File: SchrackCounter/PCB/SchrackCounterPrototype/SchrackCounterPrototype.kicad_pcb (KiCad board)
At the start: 4 copper layers, 117.5 x 98 mm, 19 parts, among them J1 Conn_01x05_Pin, SW1 SW_Push, SW2 SW_Push, SW3 SW_Push, U1 ESP32-DEVKIT-V1

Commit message: SchrackMulticlock stolen code
Not mine, I stole it, its open source
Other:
- board text added: "add buzzer"
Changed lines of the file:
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@@
 		(tags "Through hole pin header THT 1x05 2.54mm single row")
 		(property "Reference" "J1"
-			(at 0 -2.33 360)
+			(at 0 -2.33 0)
 			(layer "F.SilkS")
 			(hide yes)
@@
 		)
 		(property "Value" "Conn_01x05_Pin"
-			(at 0 12.49 360)
+			(at 0 12.49 0)
 			(layer "F.Fab")
 			(effects
@@
 		(tags "C Disc series Radial pin pitch 5.00mm  diameter 6mm width 2.5mm Capacitor")
 		(property "Reference" "C2"
-			(at 2.5 -2.5 360)
+			(at 2.5 -2.5 0)
 			(layer "F.SilkS")
 			(hide yes)
@@
 		)
 		(property "Value" "100nF"
-			(at 2.5 2.5 360)
+			(at 2.5 2.5 0)
 			(layer "F.Fab")
 			(effects
@@
 		)
 		(fp_text user "${REFERENCE}"
-			(at 2.5 0 360)
+			(at 2.5 0 0)
 			(layer "F.Fab")
 			(effects
@@
 		(tags "CP Radial series Radial pin pitch 2.50mm  diameter 6.3mm Electrolytic Capacitor")
 		(property "Reference" "C1"
-			(at 1.25 -4.4 360)
+			(at 1.25 -4.4 0)
 			(layer "F.SilkS")
 			(hide yes)
@@
 		)
 		(property "Value" "10uF"
-			(at 1.25 4.4 360)
+			(at 1.25 4.4 0)
 			(layer "F.Fab")
 			(effects
@@
 		)
 		(fp_text user "${REFERENCE}"
-			(at 1.25 0 360)
+			(at 1.25 0 0)
 			(layer "F.Fab")
 			(effects
@@
 		(tags "tact sw push 6mm")
 		(property "Reference" "SW3"
-			(at 3.25 -2.25 360)
+			(at 3.25 -2.25 0)
 			(layer "F.SilkS")
 			(hide yes)
@@
 		)
 		(property "Value" "SW_Push"
-			(at 3.75 6.7 360)
+			(at 3.75 6.7 0)
 			(layer "F.Fab")
 			(effects
@@
 		)
 		(fp_text user "${REFERENCE}"
-			(at 3.25 2.25 360)
+			(at 3.25 2.25 0)
 			(layer "F.Fab")
 			(effects
@@
 		(tags "Resistor Axial_DIN0207 series Axial Horizontal pin pitch 10.16mm 0.25W = 1/4W length 6.3mm diameter 2.5mm")
 		(property "Reference" "R4"
-			(at 5 -2.37 360)
+			(at 5 -2.37 0)
 			(layer "F.SilkS")
 			(hide yes)
@@
 		)
 		(property "Value" "1k"
-			(at 5.08 2.37 360)
+			(at 5.08 2.37 0)
 			(layer "F.Fab")
 			(effects
@@
 		)
 		(fp_text user "${REFERENCE}"
-			(at 5.08 0 360)
+			(at 5.08 0 0)
 			(layer "F.Fab")
 			(effects
@@
 		(tags "tact sw push 6mm")
 		(property "Reference" "SW2"
-			(at 3.25 -2.25 360)
+			(at 3.25 -2.25 0)
 			(layer "F.SilkS")
 			(hide yes)
@@
 		)
 		(property "Value" "SW_Push"
-			(at 3.75 6.7 360)
+			(at 3.75 6.7 0)
 			(layer "F.Fab")
 			(effects
@@
 		)
 		(fp_text user "${REFERENCE}"
-			(at 3.25 2.25 360)
+			(at 3.25 2.25 0)
 			(layer "F.Fab")
 			(effects
@@
 		(tags "C Disc series Radial pin pitch 5.00mm  diameter 6mm width 2.5mm Capacitor")
 		(property "Reference" "C3"
-			(at 2.5 -2.5 360)
+			(at 2.5 -2.5 0)
 			(layer "F.SilkS")
 			(hide yes)
@@
 		)
 		(property "Value" "100nF"
-			(at 2.5 2.5 360)
+			(at 2.5 2.5 0)
 			(layer "F.Fab")
 			(effects
@@
 		)
 		(fp_text user "${REFERENCE}"
-			(at 2.5 0 360)
+			(at 2.5 0 0)
 			(layer "F.Fab")
 			(effects
@@
 		(tags "Through hole Samtec HPM power header series 11.94mm post length THT 1x02 5.08mm single row")
 		(property "Reference" "BT1"
-			(at 8.5 0.5 360)
+			(at 8.5 0.5 0)
 			(layer "B.SilkS")
 			(hide yes)
@@
 		)
 		(property "Value" "Battery"
-			(at 0.25 2.25 360)
+			(at 0.25 2.25 0)
 			(layer "B.Fab")
 			(effects
@@
 		)
 		(fp_text user "${REFERENCE}"
-			(at 11 -1.25 360)
+			(at 11 -1.25 0)
 			(layer "B.Fab")
 			(effects
@@
 		(layer "Edge.Cuts")
 	)
+	(gr_text "add buzzer"
+		(at 189.05 123.445 0)
+		(layer "Cmts.User")
+		(effects
+			(font
+				(size 1 1)
+				(thickness 0.15)
+			)
+			(justify left bottom)
+		)
+	)
 	(dimension

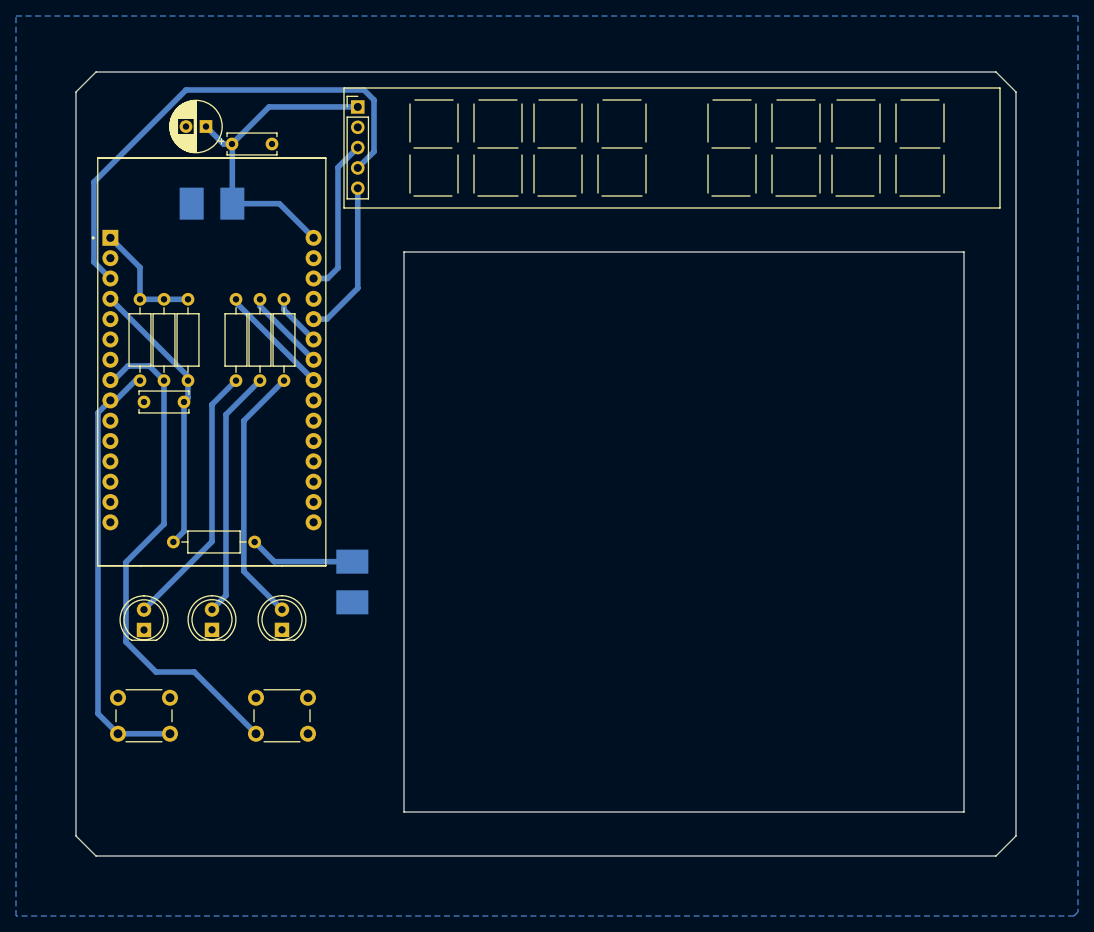
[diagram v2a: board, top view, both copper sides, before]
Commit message: Schrackcounter Prototype update
Schematic + PCB update, final version
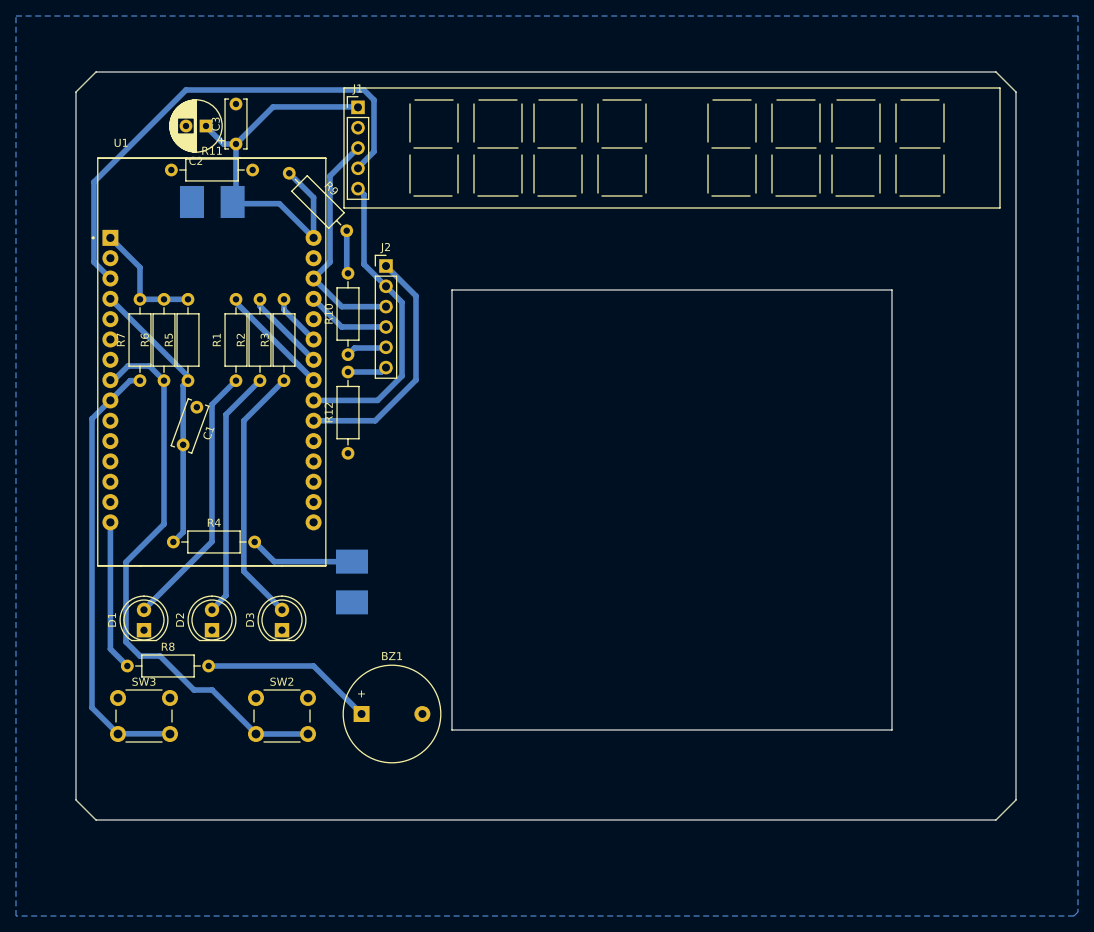
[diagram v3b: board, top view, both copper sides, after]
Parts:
- added BZ1: Buzzer, Buzzer_Beeper:Buzzer_12x9.5RM7.6, F.Cu at (176.2, 161.9)
- added J2: Conn_01x06_Pin, Connector_PinHeader_2.54mm:PinHeader_1x06_P2.54mm_Vertical, F.Cu at (179.3, 105.9)
- added R10: 0R, Resistor_THT:R_Axial_DIN0207_L6.3mm_D2.5mm_P10.16mm_Horizontal, F.Cu at (174.6, 117.0)
- added R11: 0R, Resistor_THT:R_Axial_DIN0207_L6.3mm_D2.5mm_P10.16mm_Horizontal, F.Cu at (152.5, 93.9)
- added R12: 0R, Resistor_THT:R_Axial_DIN0207_L6.3mm_D2.5mm_P10.16mm_Horizontal, F.Cu at (174.6, 129.4)
- added R8: 0R, Resistor_THT:R_Axial_DIN0207_L6.3mm_D2.5mm_P10.16mm_Horizontal, F.Cu at (147.0, 155.9)
- added R9: 0R, Resistor_THT:R_Axial_DIN0207_L6.3mm_D2.5mm_P10.16mm_Horizontal, F.Cu at (167.2, 94.4)
- C1: value 10uF -> 100nF; footprint Capacitor_THT:CP_Radial_D6.3mm_P2.50mm -> Capacitor_THT:C_Disc_D6.0mm_W2.5mm_P5.00mm
- C2: value 100nF -> 10uF; footprint Capacitor_THT:C_Disc_D6.0mm_W2.5mm_P5.00mm -> Capacitor_THT:CP_Radial_D6.3mm_P2.50mm
- moved C1 35.1 mm to (155.7, 123.6), turned to -110 degrees
- moved C3 34.2 mm to (160.6, 90.7), turned to 90 degrees
- moved C2 3.95 mm to (156.8, 88.4), turned to 180 degrees
- moved BT1 0.21 mm to (157.6, 96.4)
- moved J1 0.06 mm to (175.8, 86.1)
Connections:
- net ~{CS} renamed ~{CS0}
- C1 pad 1: +5V -> GND
- C1 pad 2: GND -> SCHRACK_SW
- C3 pad 1: GND -> +5V
- C3 pad 2: SCHRACK_SW -> GND
- U1 pad 15: unconnected-(U1-D23-Pad15) -> BZ1_PWM
- U1 pad 21: unconnected-(U1-D32-Pad21) -> ~{CS1}
- U1 pad 22: unconnected-(U1-D33-Pad22) -> CLK
- U1 pad 26: CLK -> unconnected-(U1-D14-Pad26)
- U1 pad 27: unconnected-(U1-D12-Pad27) -> MISO
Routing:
- net ~{CS1}: track 0.00 -> 30.7 mm
- net Net-(BZ1-+): track 0.00 -> 21.6 mm
- net +5V: track 41.2 -> 60.6 mm
- net BZ1_PWM: track 0.00 -> 18.8 mm
- net CLK: track 19.6 -> 38.0 mm
- net MISO: track 0.00 -> 10.5 mm
- net MOSI: track 19.7 -> 29.1 mm
- net RESET: track 63.8 -> 70.3 mm
- net GND: track 0.00 -> 5.06 mm
- net MODE: track 54.6 -> 55.2 mm
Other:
- board size 117.5 x 98 mm -> 117.5 x 93.5 mm

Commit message: Schrack prototype updated for s3
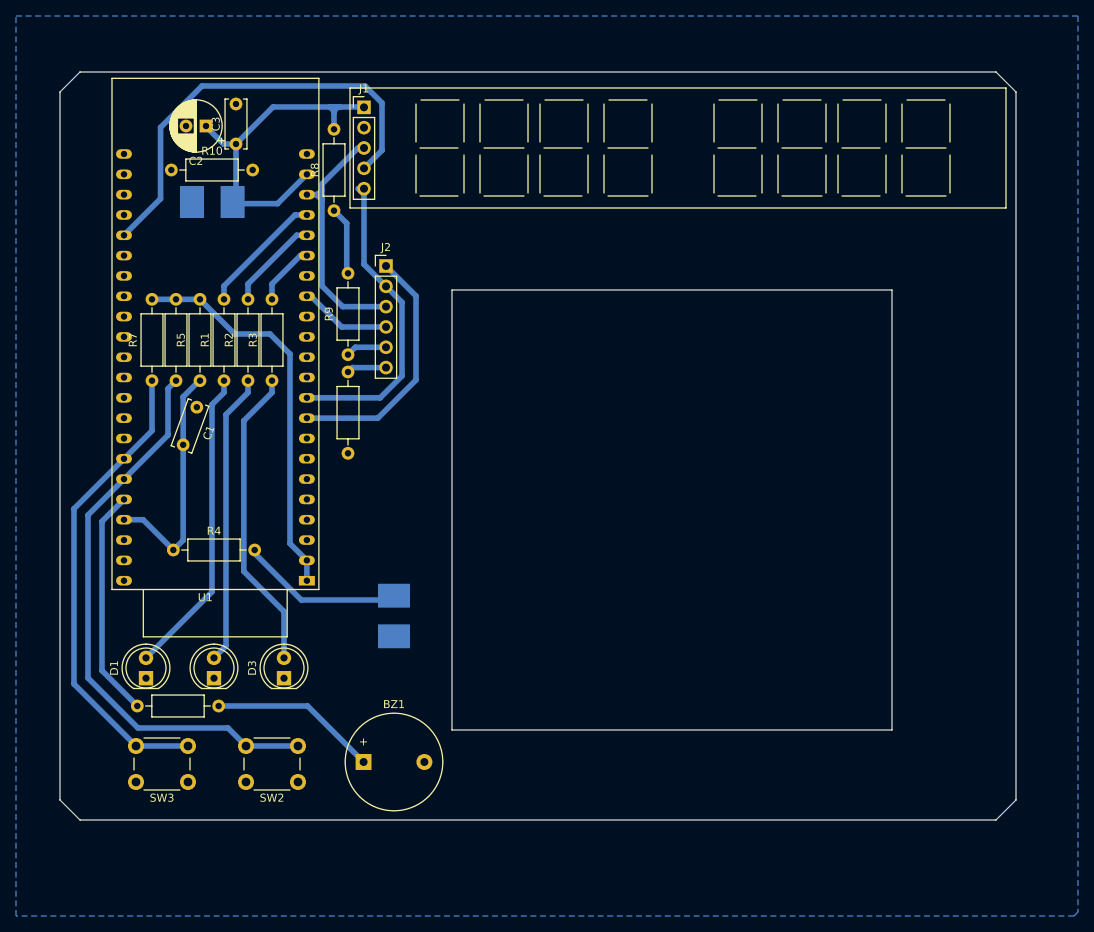
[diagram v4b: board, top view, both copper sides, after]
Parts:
- U1: value ESP32-DEVKIT-V1 -> ESP32-S3-DevKitC; footprint Schrack_brd:MODULE_ESP32_DEVKIT_V1-NoPads-NoCopper -> PCM_Espressif:ESP32-S3-DevKitC
- moved U1 29.8 mm to (169.4, 145.3), turned to 180 degrees
- moved SW3 13.7 mm to (154.6, 170.4), turned to 180 degrees
- moved SW2 11.7 mm to (168.3, 170.4), turned to 180 degrees
- moved R8 7.29 mm to (172.8, 99.0), turned to 90 degrees
- moved SW1 6.75 mm to (181.8, 149.7)
- moved BZ1 6.01 mm to (176.5, 167.9)
- moved D1 6.01 mm to (149.3, 157.5)
- moved D2 6.01 mm to (157.8, 157.5)
- moved D3 6.01 mm to (166.6, 157.5)
- moved R12 5.15 mm to (148.2, 160.9)
- moved R1 1.50 mm to (159.1, 120.3)
- moved R2 1.50 mm to (162.1, 120.3)
- moved R3 1.50 mm to (165.1, 120.3)
- moved R5 1.50 mm to (156.1, 120.3)
- moved R6 1.50 mm to (153.1, 120.3)
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- renumbered R11 to R10, R12 to R11, R8 to R12, R9 to R8, R10 to R9
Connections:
- U1 pad 10: unconnected-(U1-D19-Pad10) -> CLK
- U1 pad 15: BZ1_PWM -> MISO
- U1 pad 17: unconnected-(U1-VP-Pad17) -> LED_EXT3
- U1 pad 18: unconnected-(U1-VN-Pad18) -> LED_EXT2
- U1 pad 19: unconnected-(U1-D34-Pad19) -> LED_EXT1
- U1 pad 2: GND -> +3V3
- U1 pad 20: unconnected-(U1-D35-Pad20) -> MOSI
- U1 pad 21: ~{CS1} -> +5V
- U1 pad 22: CLK -> GND
- U1 pad 23: LED_EXT1 -> GND
- U1 pad 24: LED_EXT2 -> GND
- U1 pad 25: LED_EXT3 -> unconnected-(U1-GPIO19/USB_D--Pad25)
- U1 pad 27: MISO -> ~{CS0}
- U1 pad 28: MOSI -> unconnected-(U1-GPIO47-Pad28)
- U1 pad 29: GND -> unconnected-(U1-GPIO48-Pad29)
- U1 pad 3: ~{CS0} -> unconnected-(U1-CHIP_PU-Pad3)
- U1 pad 30: +5V -> unconnected-(U1-GPIO45-Pad30)
- U1 pad 4: SCHRACK_SW -> unconnected-(U1-GPIO4/ADC1_CH3-Pad4)
- U1 pad 8: RESET -> unconnected-(U1-GPIO15/ADC2_CH4/32K_P-Pad8)
- U1 pad 9: MODE -> ~{CS1}
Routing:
- net +3V3: track 15.2 -> 49.3 mm
- net BZ1_PWM: track 18.8 -> 28.8 mm
- net ~{CS0}: track 62.5 -> 55.2 mm
- net Net-(R4-Pad2): track 13.2 -> 20.5 mm
- net Net-(D3-A): track 32.7 -> 38.2 mm
- net Net-(D2-A): track 31.1 -> 36.4 mm
- net Net-(D1-A): track 33.4 -> 38.7 mm
- net SCHRACK_SW: track 35.2 -> 30.3 mm
- net MODE: track 55.2 -> 59.4 mm
- net MOSI: track 29.1 -> 32.8 mm
- net +5V: track 60.6 -> 57.9 mm
- net LED_EXT1: track 14.1 -> 15.7 mm
- net LED_EXT2: track 10.3 -> 11.8 mm
- net LED_EXT3: track 6.55 -> 7.75 mm
- net RESET: track 70.3 -> 71.5 mm
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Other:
- board size 117.5 x 93.5 mm -> 119.5 x 93.5 mm

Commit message: Multiclock PCB update
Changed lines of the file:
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@@
 		(grid_origin 143.05 179.695)
 		(pcbplotparams
-			(layerselection 0x00010fc_ffffffff)
+			(layerselection 0x0001000_fffffff8)
 			(plot_on_all_layers_selection 0x0000000_00000000)
 			(disableapertmacros no)
@@
 			(svgprecision 4)
 			(plotframeref no)
-			(viasonmask no)
+			(viasonmask yes)
 			(mode 1)
-			(useauxorigin no)
+			(useauxorigin yes)
 			(hpglpennumber 1)
 			(hpglpenspeed 20)
@@
 			(psnegative no)
 			(psa4output no)
-			(plotreference yes)
-			(plotvalue yes)
-			(plotfptext yes)
+			(plotreference no)
+			(plotvalue no)
+			(plotfptext no)
 			(plotinvisibletext no)
 			(sketchpadsonfab no)
@@
 			(outputformat 1)
 			(mirror no)
-			(drillshape 1)
+			(drillshape 0)
 			(scaleselection 1)
 			(outputdirectory "")
@@
 		(tags "tact sw push 6mm")
 		(property "Reference" "SW3"
-			(at 3.25 -2 360)
+			(at 3.25 -2 0)
 			(layer "F.SilkS")
 			(effects
@@
 		)
 		(property "Value" "SW_Push"
-			(at 3.75 6.7 360)
+			(at 3.75 6.7 0)
 			(layer "F.Fab")
 			(effects
@@
 		)
 		(fp_text user "${REFERENCE}"
-			(at 3.25 2.25 360)
+			(at 3.25 2.25 0)
 			(layer "F.Fab")
 			(effects
@@
 		(tags "tact sw push 6mm")
 		(property "Reference" "SW2"
-			(at 3.25 -2 360)
+			(at 3.25 -2 0)
 			(layer "F.SilkS")
 			(effects
@@
 		)
 		(property "Value" "SW_Push"
-			(at 3.75 6.7 360)
+			(at 3.75 6.7 0)
 			(layer "F.Fab")
 			(effects
@@
 		)
 		(fp_text user "${REFERENCE}"
-			(at 3.25 2.25 360)
+			(at 3.25 2.25 0)
 			(layer "F.Fab")
 			(effects
@@
 		(tags "ESP32-S3")
 		(property "Reference" "U1"
-			(at 12.7 -2.1 360)
+			(at 12.7 -2.1 0)
 			(layer "F.SilkS")
 			(effects
@@
 		)
 		(property "Footprint" "PCM_Espressif:ESP32-S3-DevKitC"
-			(at 0 0 360)
+			(at 0 0 0)
 			(layer "F.Fab")
 			(hide yes)
@@
 		)
 		(property "Datasheet" ""
-			(at 0 0 360)
+			(at 0 0 0)
 			(layer "F.Fab")
 			(hide yes)
@@
 		)
 		(property "Description" "ESP32-S3-DevKitC"
-			(at 0 0 360)
+			(at 0 0 0)
 			(layer "F.Fab")
 			(hide yes)
@@
 		)
 		(fp_text user "REF**"
-			(at -0.00368 -0.00272 360)
+			(at -0.00368 -0.00272 0)
 			(layer "F.Fab")
 			(effects
@@
 		(layer "Dwgs.User")
 		(pts
-			(xy 256.3 81.695) (xy 256.3 179.695)
+			(xy 255.55 81.695) (xy 255.55 175.195)
+		)
+		(height -36)
+		(gr_text "93.5000 mm"
+			(at 290.4 128.445 90)
+			(layer "Dwgs.User")
+			(effects
+				(font
+					(size 1 1)
+					(thickness 0.15)
+				)
+			)
+		)
+		(format
+			(prefix "")
+			(suffix "")
+			(units 3)
+			(units_format 1)
+			(precision 4)
+		)
+		(style
+			(thickness 0.15)
+			(arrow_length 1.27)
+			(text_position_mode 0)
+			(extension_height 0.58642)
+			(extension_offset 0.5) keep_text_aligned)
+	)
+	(dimension
+		(type aligned)
+		(layer "Dwgs.User")
+		(pts
+			(xy 258.05 84.195) (xy 138.55 84.195)
 		)
-		(height -19.5)
-		(gr_text "98 mm"
-			(at 274.65 130.695 90)
+		(height 21.749999)
+		(gr_text "119.5000 mm"
+			(at 198.3 61.295001 0)
 			(layer "Dwgs.User")
 			(effects
@@
 			(units 3)
 			(units_format 1)
-			(precision 4) suppress_zeroes)
+			(precision 4)
+		)
 		(style
 			(thickness 0.15)
@@
 	)
 	(segment
-		(start 149.3 154.93)
-		(end 157.55 146.68)
-		(width 0.7)
-		(layer "B.Cu")
-		(net 4)
-	)
-	(segment
 		(start 157.55 146.68)
 		(end 157.55 123.27)
@@
 	)
 	(segment
-		(start 162.05 121.77)
-		(end 159.3 124.52)
+		(start 149.3 154.93)
+		(end 157.55 146.68)
 		(width 0.7)
 		(layer "B.Cu")
-		(net 5)
+		(net 4)
 	)
 	(segment
-		(start 159.3 153.43)
-		(end 157.8 154.93)
+		(start 159.3 148.195)
+		(end 157.8 149.695)
 		(width 0.7)
 		(layer "B.Cu")
@@
 	)
 	(segment
-		(start 159.3 124.52)
-		(end 159.3 153.43)
+		(start 162.05 121.77)
+		(end 159.3 124.52)
 		(width 0.7)
 		(layer "B.Cu")
@@
 	)
 	(segment
-		(start 166.55 149.135)
-		(end 161.53 144.115)
+		(start 157.8 149.695)
+		(end 157.8 154.93)
 		(width 0.7)
 		(layer "B.Cu")
-		(net 6)
+		(net 5)
 	)
 	(segment
-		(start 166.55 154.93)
-		(end 166.55 149.135)
+		(start 159.3 124.52)
+		(end 159.3 148.195)
 		(width 0.7)
 		(layer "B.Cu")
-		(net 6)
+		(net 5)
 	)
 	(segment
@@
 	)
 	(segment
+		(start 166.55 154.93)
+		(end 161.53 149.91)
+		(width 0.7)
+		(layer "B.Cu")
+		(net 6)
+	)
+	(segment
 		(start 165.05 121.77)
 		(end 165.05 120.275)
@@
 	)
 	(segment
-		(start 161.53 144.115)
+		(start 161.53 149.91)
 		(end 161.53 125.29)
 		(width 0.7)
@@
 	)
 	(segment
-		(start 165.05 108.195)
-		(end 165.05 110.115)
+		(start 168.6 104.645)
+		(end 165.05 108.195)
 		(width 0.7)
 		(layer "B.Cu")
@@
 	)
 	(segment
-		(start 169.41 104.645)
-		(end 168.6 104.645)
+		(start 165.05 108.195)
+		(end 165.05 110.115)
 		(width 0.7)
 		(layer "B.Cu")
@@
 	)
 	(segment
-		(start 168.6 104.645)
-		(end 165.05 108.195)
+		(start 169.41 104.645)
+		(end 168.6 104.645)
 		(width 0.7)
 		(layer "B.Cu")
